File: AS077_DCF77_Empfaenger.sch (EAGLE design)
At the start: 81 parts, among them IC1 4093N, IC2 4538N, IC3 CA3130E, IC4 4093N, J1 Rückkopplung, J2 JUMPER_J5MM, J3 JUMPER_J5MM, Q1 BF 244A, Q2 BC549C, Q3 BC549, Q4 TRANSISTOR-NPN_BC2385.08, Q5 BC549C, Q6 TRANSISTOR-PNP_BC2145.08, Q7 BC549C

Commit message: * Added "bottom capacitor" * Added nets and polygons to not connected IC pins
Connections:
- new net N$45: IC2A.Q
- new net N$46: IC3.ON
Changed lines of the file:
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@@
+</segment>
+</net>
+<net name="N$45" class="0">
+<segment>
+<pinref part="IC2" gate="A" pin="Q"/>
+<wire x1="152.4" y1="116.84" x2="154.94" y2="116.84" width="0.1524" layer="91"/>
+</segment>
+</net>
+<net name="N$46" class="0">
+<segment>
+<pinref part="IC3" gate="A" pin="ON"/>
+<wire x1="218.44" y1="218.44" x2="218.44" y2="215.9" width="0.1524" layer="91"/>
 </segment>
 </net>

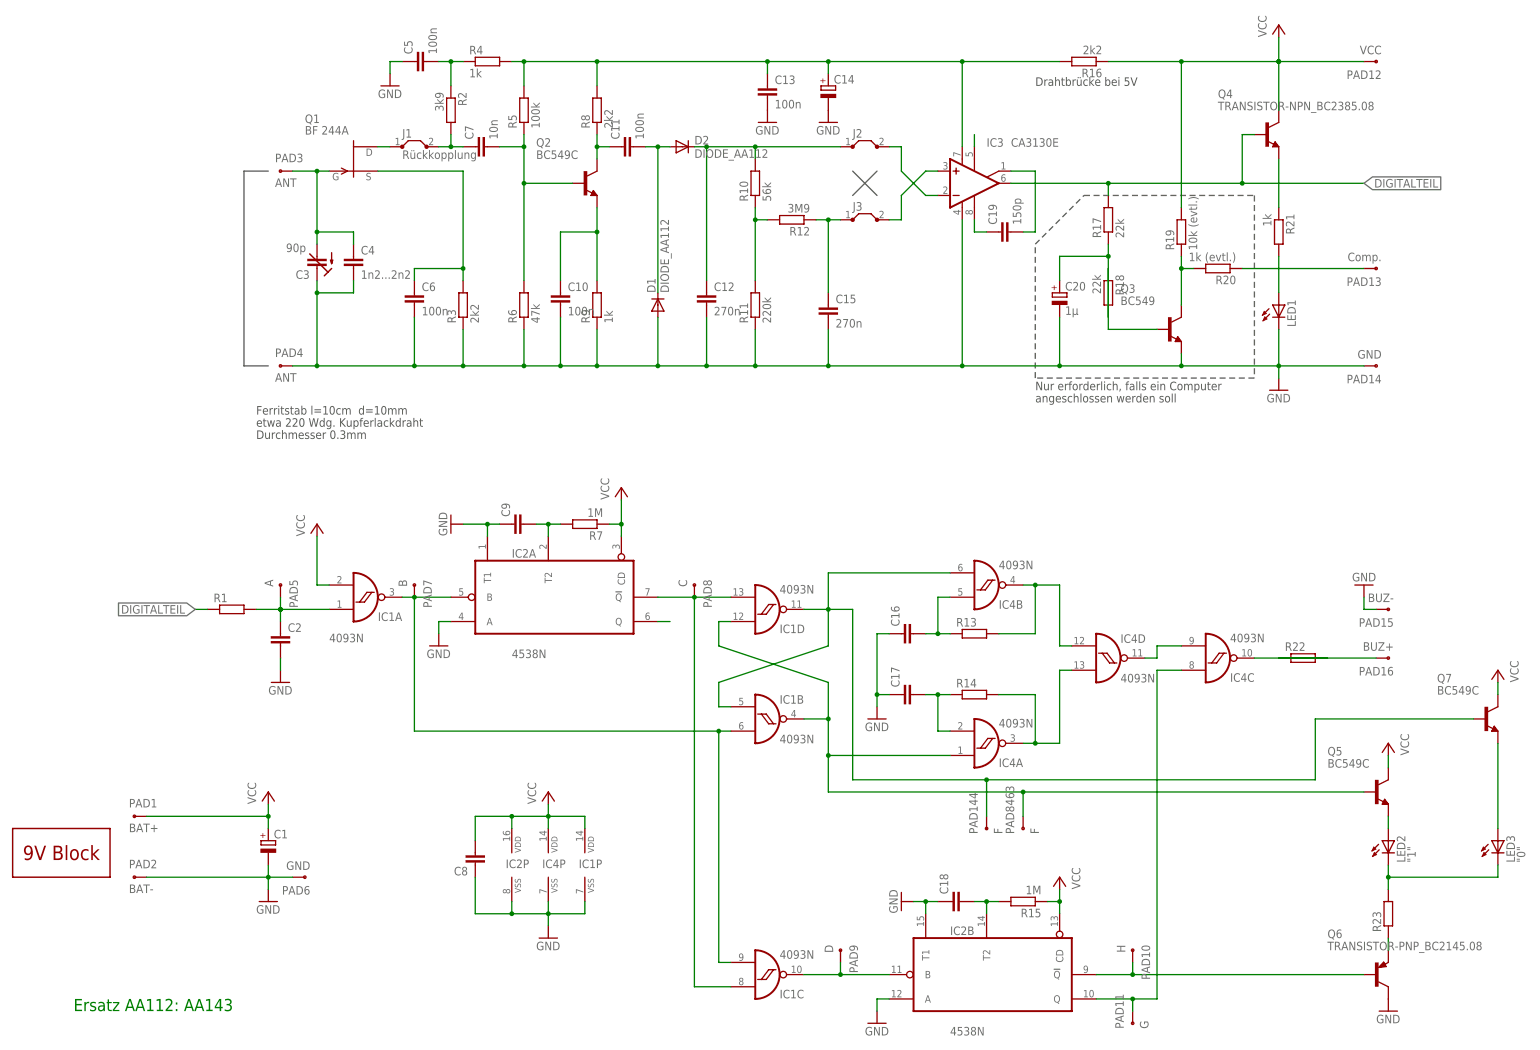
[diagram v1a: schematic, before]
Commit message: * Added more details to the silkscreen * Fixed all Values in schematic
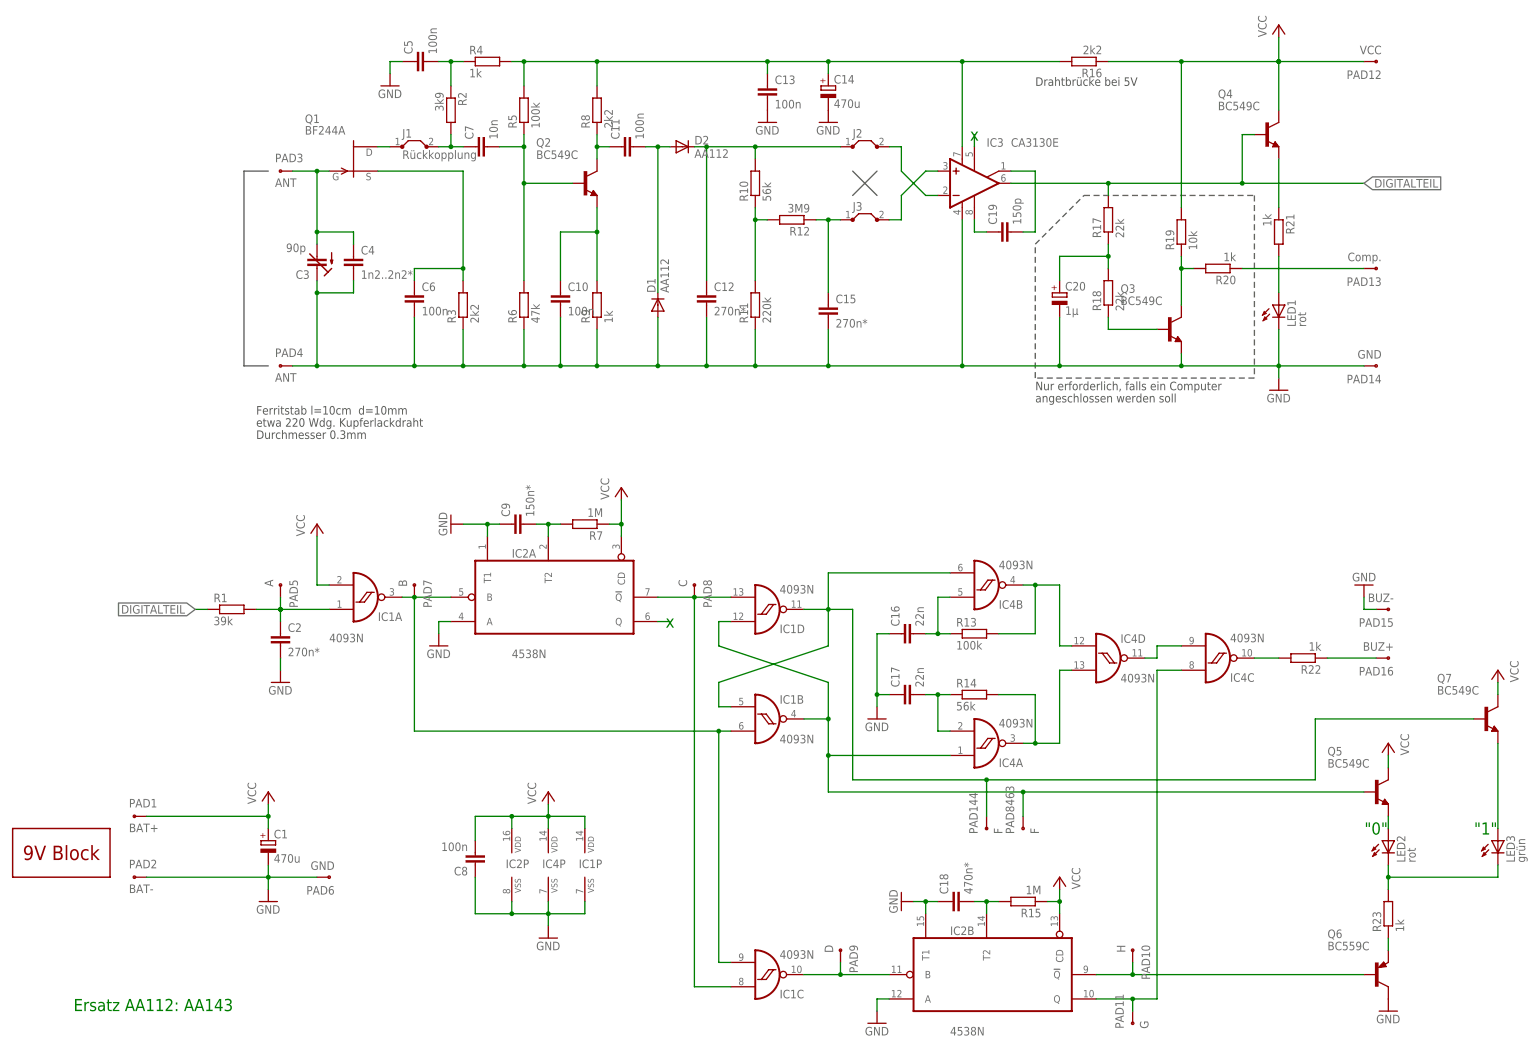
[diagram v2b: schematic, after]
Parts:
- C1, C14: value (none) -> 470u
- C12, C15: value 270n -> 270n*
- C16, C17: value (none) -> 22n
- C18: value (none) -> 470n*
- C2: value (none) -> 270n*
- C4: value 1n2...2n2 -> 1n2..2n2*
- C8: value (none) -> 100n
- C9: value (none) -> 150n*
- D1, D2: value DIODE_AA112 -> AA112
- LED1: value (none) -> rot
- LED2: value "1" -> rot
- LED3: value "0" -> grün
- Q1: value BF 244A -> BF244A
- Q3: value BC549 -> BC549C
- Q4: value TRANSISTOR-NPN_BC2385.08 -> BC549C
- Q6: value TRANSISTOR-PNP_BC2145.08 -> BC559C
- R1: value (none) -> 39k
- R13: value (none) -> 100k
- R14: value (none) -> 56k
- R19: value 10k (evtl.) -> 10k
- R20: value 1k (evtl.) -> 1k
- R22, R23: value (none) -> 1k
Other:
- note added: ""0""
- note added: ""1""
- note added: "x"
- moved on the sheet: PAD6, R18, R22

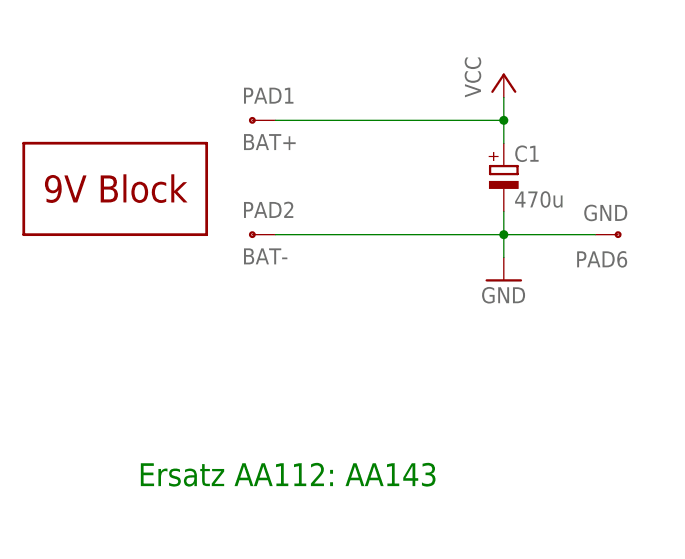
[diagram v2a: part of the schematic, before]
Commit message: * more silkscreen improvements * added GERBER
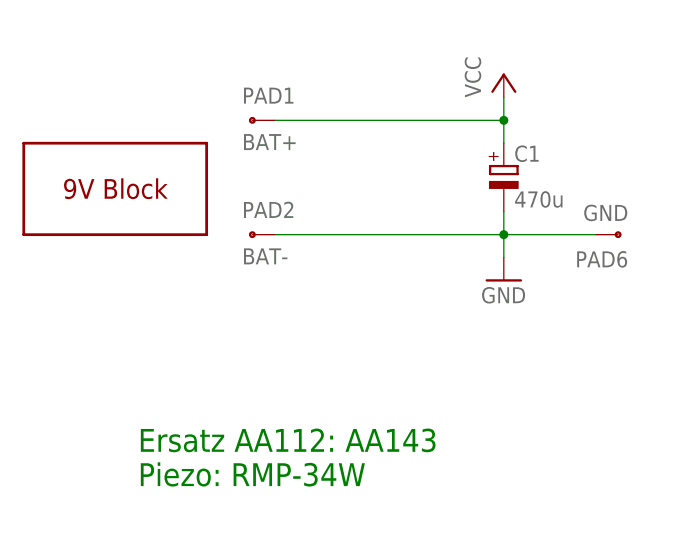
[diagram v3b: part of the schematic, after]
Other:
- note added: "Ersatz AA112: AA143 Piezo: RMP-34W"
- note removed: "Ersatz AA112: AA143"
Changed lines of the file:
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@@
 <text x="68.58" y="154.94" size="1.778" layer="97">Durchmesser 0.3mm</text>
 <text x="231.14" y="228.6" size="1.778" layer="97">Drahtbrücke bei 5V</text>
-<text x="30.48" y="35.56" size="2.54" layer="91">Ersatz AA112: AA143</text>
+<text x="30.48" y="35.56" size="2.54" layer="91">Ersatz AA112: AA143
+Piezo: RMP-34W</text>
 <text x="154.94" y="116.84" size="2.54" layer="91" align="center">x</text>
 <text x="218.44" y="218.44" size="2.54" layer="91" align="center">x</text>
@@
 </drawing>
 <compatibility>
+<note version="6.3" minversion="6.2.2" severity="warning">
+Since Version 6.2.2 text objects can contain more than one line,
+which will not be processed correctly with this version.
+</note>
 <note version="8.2" severity="warning">
 Since Version 8.2, EAGLE supports online libraries. The ids
